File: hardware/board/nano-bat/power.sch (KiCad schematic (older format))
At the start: 26 parts, among them Q501 Q_PMOS_GSD, Q502 Q_NMOS_GSD, Q503 Q_NMOS_GSD, U501 MIC2104YML-TR, U502 MCP1702

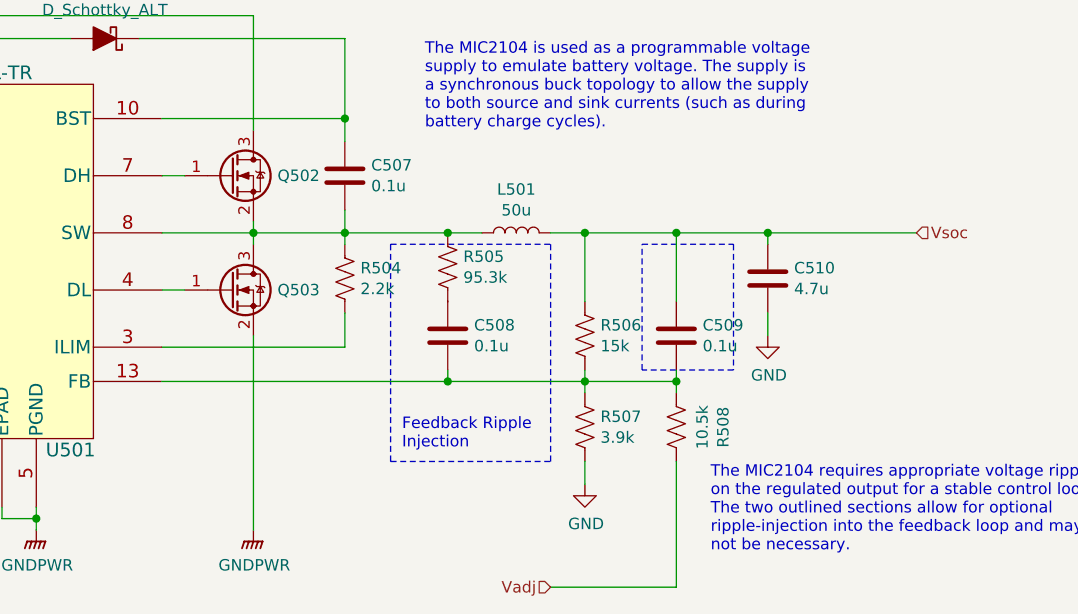
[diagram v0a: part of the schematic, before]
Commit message: Adding test points, initial board outline
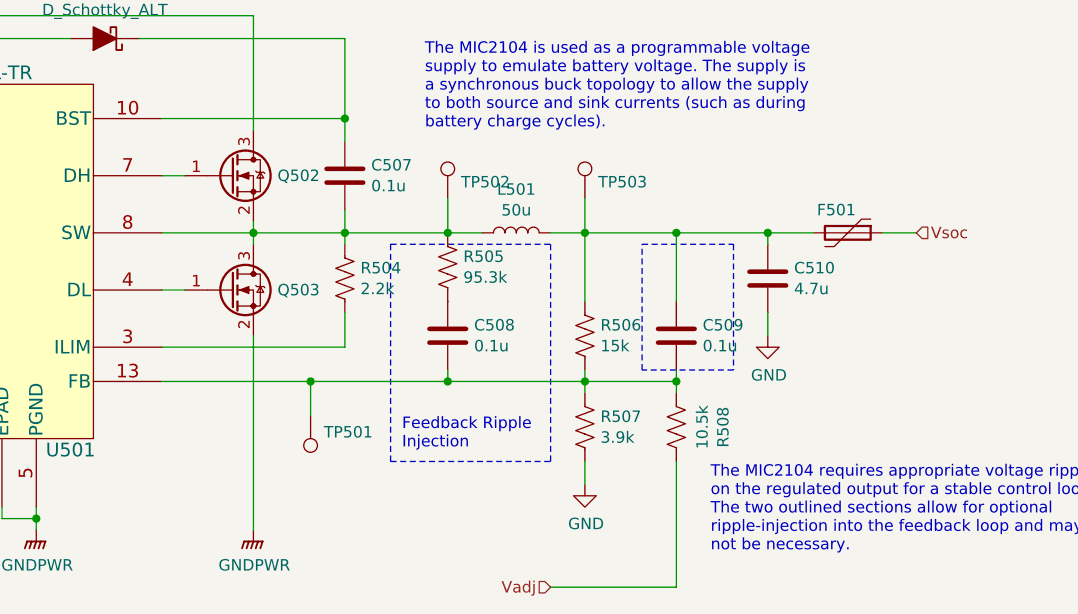
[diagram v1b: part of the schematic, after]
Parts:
- added F501: Polyfuse, Fuse:Fuse_1812_4532Metric, symbol Device:Polyfuse
- added TP501, TP502, TP503: TestPoint, TestPoint:TestPoint_Pad_D1.0mm, symbol Connector:TestPoint
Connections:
- net Vsoc: now also F501.1; no longer C509.1, C510.1, L501.2, R506.2
- net at C508.2, C509.2, R506.1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: now also TP501.1
- net at C507.2, L501.1, Q502.2 (S)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: now also TP502.1
- new net: C509.1, C510.1, F501.2, L501.2, R506.2, TP503.1
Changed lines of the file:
@@
 	7550 3650 7550 3600
 Wire Wire Line
-	7550 3650 6300 3650
+	7550 3650 6950 3650
 Connection ~ 7550 3650
 Wire Wire Line
@@
 $EndComp
 Wire Wire Line
-	8950 3000 9600 3000
+	8950 3000 9150 3000
 $Comp
 L power:GND #PWR0501
@@
 Text Notes 2950 1900 0    50   ~ 0
 The MIC2104 provides a 5V LDO output on VDD that \ncan be shorted to PVDD to drive the power-switch \nMOSFET drivers. Under conditions where VIN is less \nthan 5.5V, the 5V LDO needs to be bypassed as it won't \nbe able to maintain regulation. A FET is used to connect \nVIN to VDD (and bypass the internal LDO) whenever \npower is not applied to the barrel-jack connector.
+$Comp
+L Device:Polyfuse F?
+U 1 1 5E1D5B5B
+P 9300 3000
+AR Path="/5E1D5B5B" Ref="F?"  Part="1"
+AR Path="/5DD44E3C/5E1D5B5B" Ref="F501"  Part="1"
+F 0 "F501" V 9200 2950 50  0000 C CNN
+F 1 "Polyfuse" V 9200 2950 50  0001 C CNN
+F 2 "Fuse:Fuse_1812_4532Metric" H 9350 2800 50  0001 L CNN
+F 3 "~" H 9300 3000 50  0001 C CNN
+F 4 "507-1763-1-ND" V 9300 3000 50  0001 C CNN "Part"
+	1    9300 3000
+	0    1    1    0
+$EndComp
+Wire Wire Line
+	9450 3000 9600 3000
+$Comp
+L Connector:TestPoint TP501
+U 1 1 5E31CD10
+P 6950 3800
+F 0 "TP501" H 6892 3872 50  0000 R CNN
+F 1 "TestPoint" H 6892 3917 50  0001 R CNN
+F 2 "TestPoint:TestPoint_Pad_D1.0mm" H 7150 3800 50  0001 C CNN
+F 3 "~" H 7150 3800 50  0001 C CNN
+	1    6950 3800
+	-1   0    0    1
+$EndComp
+Wire Wire Line
+	6950 3800 6950 3650
+Connection ~ 6950 3650
+Wire Wire Line
+	6950 3650 6300 3650
+$Comp
+L Connector:TestPoint TP502
+U 1 1 5E320F38
+P 7550 2850
+F 0 "TP502" H 7608 2922 50  0000 L CNN
+F 1 "TestPoint" H 7492 2967 50  0001 R CNN
+F 2 "TestPoint:TestPoint_Pad_D1.0mm" H 7750 2850 50  0001 C CNN
+F 3 "~" H 7750 2850 50  0001 C CNN
+	1    7550 2850
+	1    0    0    -1
+$EndComp
+Wire Wire Line
+	7550 2850 7550 3000
+$Comp
+L Connector:TestPoint TP503
+U 1 1 5E324C2D
+P 8150 2850
+F 0 "TP503" H 8208 2922 50  0000 L CNN
+F 1 "TestPoint" H 8092 2967 50  0001 R CNN
+F 2 "TestPoint:TestPoint_Pad_D1.0mm" H 8350 2850 50  0001 C CNN
+F 3 "~" H 8350 2850 50  0001 C CNN
+	1    8150 2850
+	1    0    0    -1
+$EndComp
+Wire Wire Line
+	8150 2850 8150 3000
 $EndSCHEMATC
